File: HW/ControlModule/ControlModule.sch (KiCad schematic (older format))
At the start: 12 parts

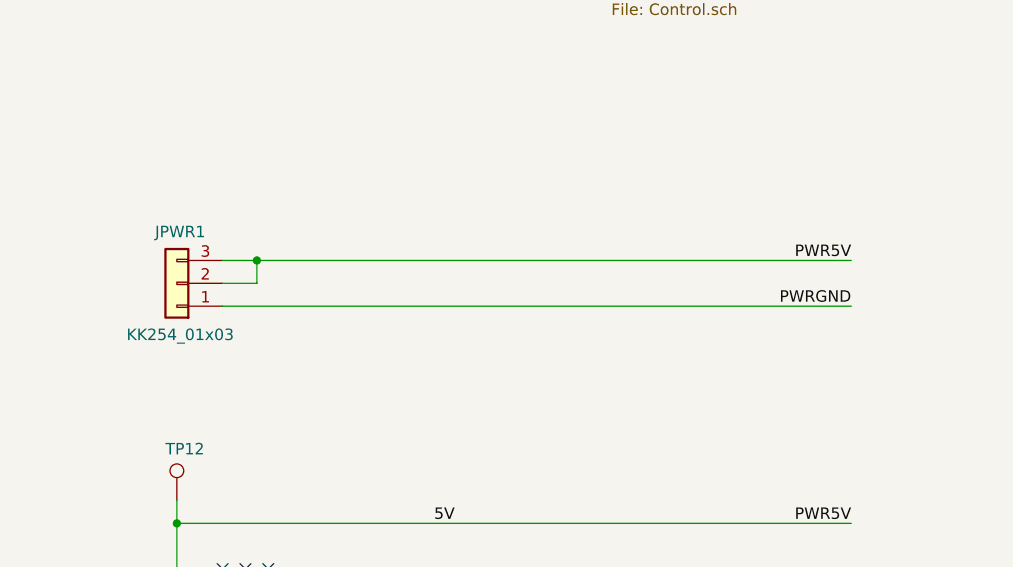
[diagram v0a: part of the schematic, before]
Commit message: Added Interafec IBOMS
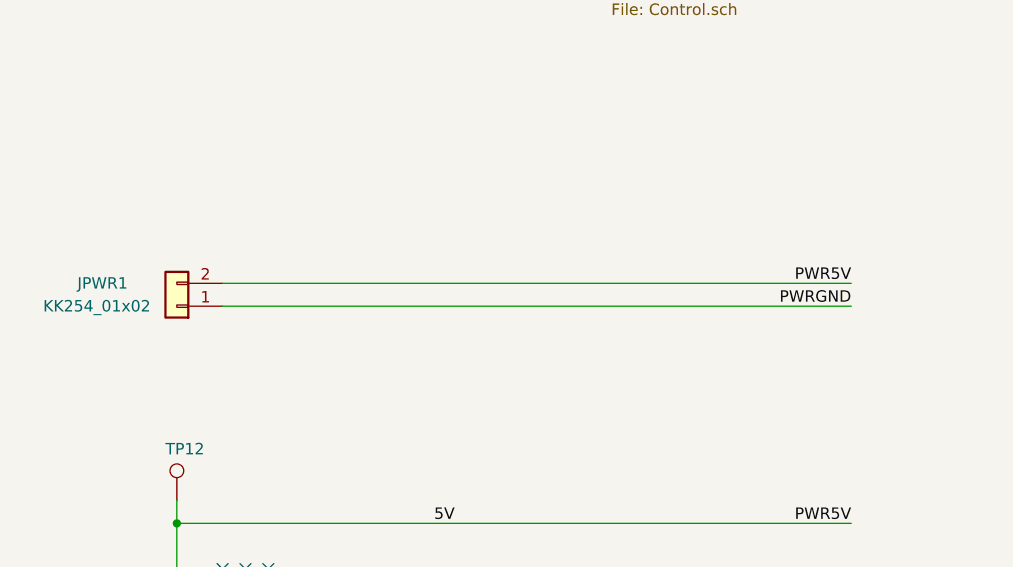
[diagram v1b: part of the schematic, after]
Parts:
- removed JPWR1: KK254_01x03, Connector_Molex:Molex_KK-254_AE-6410-03A_1x03_P2.54mm_Vertical, symbol Connector_Generic:Conn_01x03
- added JPWR1: KK254_01x02, Connector_Molex:Molex_KK-254_AE-6410-02A_1x02_P2.54mm_Vertical, symbol Connector_Generic:Conn_01x02
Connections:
- net 5V: now also JPWR1.2 (Pin_2)
- net PWRGND: now also JPWR1.1 (Pin_1)
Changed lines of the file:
@@
 Wire Wire Line
 	2550 3000 2550 3100
-$Comp
-L Connector_Generic:Conn_01x03 JPWR1
-U 1 1 5CAE97C0
-P 2150 4950
-F 0 "JPWR1" H 2025 4725 50  0000 L CNN
-F 1 "KK254_01x03" H 1900 5175 50  0000 L CNN
-F 2 "Connector_Molex:Molex_KK-254_AE-6410-03A_1x03_P2.54mm_Vertical" H 2150 4950 50  0001 C CNN
-F 3 "~" H 2150 4950 50  0001 C CNN
-F 4 "WM4201-ND" H 2150 4950 50  0001 C CNN "DigikeyNo"
-	1    2150 4950
-	-1   0    0    1
-$EndComp
-Wire Wire Line
-	2350 4850 2500 4850
 Wire Wire Line
 	7950 2800 9000 2800
@@
 Text Label 5100 5050 2    50   ~ 0
 PWRGND
-Text Label 5100 4850 2    50   ~ 0
+Text Label 5100 4950 2    50   ~ 0
 PWR5V
-Wire Wire Line
-	2350 4950 2500 4950
-Wire Wire Line
-	2500 4950 2500 4850
-Connection ~ 2500 4850
-Wire Wire Line
-	2500 4850 5100 4850
 $Comp
 L Device:D_Schottky D?
@@
 Wire Wire Line
 	2750 6500 4050 6500
+$Comp
+L Connector_Generic:Conn_01x02 JPWR1
+U 1 1 5D504877
+P 2150 5050
+F 0 "JPWR1" H 2475 4950 50  0000 C CNN
+F 1 "KK254_01x02" H 2500 5050 50  0000 C CNN
+F 2 "Connector_Molex:Molex_KK-254_AE-6410-02A_1x02_P2.54mm_Vertical" H 2150 5050 50  0001 C CNN
+F 3 "~" H 2150 5050 50  0001 C CNN
+	1    2150 5050
+	-1   0    0    1
+$EndComp
+Wire Wire Line
+	2350 4950 5100 4950
 $EndSCHEMATC
